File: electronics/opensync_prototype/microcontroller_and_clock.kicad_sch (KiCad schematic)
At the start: 42 parts, among them U2 RP2354_80QFN

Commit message: Backup push
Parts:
- added C? (x2): C, symbol Device:C
- added R?: 1k, symbol Device:R
- added Y?: ABM8-272-T3, ABM8-272-T3:XTAL_ABM8-272-T3, symbol ABM8-272-T3:ABM8-272-T3
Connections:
- net GND: now also Y?.2 (GND), Y?.4 (GND)
- net XIN: now also C?.2, Y?.1
- net XOUT: now also R?.2
- new net: C?.1, C?.1
- new net: C?.2, R?.1, Y?.3
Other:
- note added: "12 MHz Cystal Oscillator"
- note added: "Push Button Boot Select"
- note added: "Push Button Reset"

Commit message: KiCAD backup
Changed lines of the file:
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@@
 	(text "12 MHz Cystal Oscillator"
 		(exclude_from_sim no)
-		(at 41.656 124.968 0)
+		(at 39.624 130.81 0)
 		(effects
 			(font

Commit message: Emergency backup
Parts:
- C10, C11, C12, C13, C14, C15, C16, C17, C2, C3, C6, C7, C8, C9: renamed from C?; footprint (none) -> RP2350_80QFN_minimal:C_0402_1005Metric_small_pads
- C5: renamed from C?; footprint Capacitor_SMD:C_0402_1005Metric -> RP2350_80QFN_minimal:C_0402_1005Metric_small_pads
- L1: renamed from L?; footprint RP2350_80QFN_minimal:L_pol_2016 -> Resistor_SMD:R_0402_1005Metric
- R2: renamed from R?; footprint (none) -> Resistor_SMD:R_0402_1005Metric
- gave numbers to parts that had none: 28

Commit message: Backup copy
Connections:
- net CLOCK_1: now also U2.1 (GPIO4); no longer U2.77 (GPIO0)
- net CLOCK_2: now also U2.2 (GPIO5); no longer U2.78 (GPIO1)
- net CLOCK_3: now also U2.3 (GPIO6); no longer U2.79 (GPIO2)
- net OUTPUT_1: now also U2.21 (GPIO21); no longer U2.6 (GPIO8)
- net OUTPUT_10: now also U2.38 (GPIO30); no longer U2.17 (GPIO17)
- net OUTPUT_11: now also U2.39 (GPIO31); no longer U2.18 (GPIO18)
- net OUTPUT_12: now also U2.40 (GPIO32); no longer U2.19 (GPIO19)
- net OUTPUT_2: now also U2.22 (GPIO22); no longer U2.7 (GPIO9)
- net OUTPUT_3: now also U2.23 (GPIO23); no longer U2.8 (GPIO10)
- net OUTPUT_4: now also U2.25 (GPIO24); no longer U2.9 (GPIO11)
- net OUTPUT_5: now also U2.26 (GPIO25); no longer U2.11 (GPIO12)
- net OUTPUT_6: now also U2.27 (GPIO26); no longer U2.12 (GPIO13)
- net OUTPUT_7: now also U2.28 (GPIO27); no longer U2.13 (GPIO14)
- net OUTPUT_8: now also U2.36 (GPIO28); no longer U2.14 (GPIO15)
- net OUTPUT_9: now also U2.37 (GPIO29); no longer U2.16 (GPIO16)
- net TRIGGER_1: now also U2.18 (GPIO18); no longer U2.1 (GPIO4)
- net TRIGGER_2: now also U2.19 (GPIO19); no longer U2.2 (GPIO5)
- net TRIGGER_3: now also U2.20 (GPIO20); no longer U2.3 (GPIO6)
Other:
- moved on the sheet: R10, R5, R6, R7, R8, R9

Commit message: Emergency backup
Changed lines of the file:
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@@
+		)
+	)
+	(label "OUTPUT_7"
+		(at 172.72 118.11 0)
+		(effects
+			(font
+				(size 1.27 1.27)
+			)
+			(justify left bottom)
+		)
+	)
+	(label "OUTPUT_1"
+		(at 172.72 102.87 0)
+		(effects
+			(font
+				(size 1.27 1.27)
+			)
+			(justify left bottom)
 		)
 	)
@@
 		)
 	)
+	(label "OUTPUT_3"
+		(at 172.72 107.95 0)
+		(effects
+			(font
+				(size 1.27 1.27)
+			)
+			(justify left bottom)
+		)
+	)
+	(label "OUTPUT_5"
+		(at 172.72 113.03 0)
+		(effects
+			(font
+				(size 1.27 1.27)
+			)
+			(justify left bottom)
+		)
+	)
 	(label "CLOCK_2"
 		(at 171.45 62.23 0)
@@
 		)
 	)
+	(label "OUTPUT_2"
+		(at 172.72 105.41 0)
+		(effects
+			(font
+				(size 1.27 1.27)
+			)
+			(justify left bottom)
+		)
+	)
 	(label "RUN"
 		(at 93.98 102.87 0)
@@
 		)
 	)
+	(label "OUTPUT_6"
+		(at 172.8998 115.57 0)
+		(effects
+			(font
+				(size 1.27 1.27)
+			)
+			(justify left bottom)
+		)
+	)
 	(label "QSPL_SS"
 		(at 92.71 60.96 0)
@@
 		)
 	)
+	(label "OUTPUT_9"
+		(at 172.72 123.19 0)
+		(effects
+			(font
+				(size 1.27 1.27)
+			)
+			(justify left bottom)
+		)
+	)
+	(label "TRIGGER_1"
+		(at 172.72 95.25 0)
+		(effects
+			(font
+				(size 1.27 1.27)
+			)
+			(justify left bottom)
+		)
+	)
 	(label "XIN"
 		(at 66.04 135.89 0)
@@
 		)
 	)
+	(label "OUTPUT_12"
+		(at 172.72 130.81 0)
+		(effects
+			(font
+				(size 1.27 1.27)
+			)
+			(justify left bottom)
+		)
+	)
+	(label "OUTPUT_4"
+		(at 172.72 110.49 0)
+		(effects
+			(font
+				(size 1.27 1.27)
+			)
+			(justify left bottom)
+		)
+	)
 	(label "CLOCK_3"
 		(at 171.45 64.77 0)
@@
 		(effects
 			(font
+				(size 1.27 1.27)
+			)
+			(justify left bottom)
+		)
+	)
+	(label "TRIGGER_3"
+		(at 172.72 100.33 0)
+		(effects
+			(font
+				(size 1.27 1.27)
+			)
+			(justify left bottom)
+		)
+	)
+	(label "OUTPUT_11"
+		(at 172.72 128.27 0)
+		(effects
+			(font
+				(size 1.27 1.27)
+			)
+			(justify left bottom)
+		)
+	)
+	(label "TRIGGER_2"
+		(at 172.72 97.79 0)
+		(effects
+			(font
+				(size 1.27 1.27)
+			)
+			(justify left bottom)
+		)
+	)
+	(label "OUTPUT_8"
+		(at 172.8453 120.65 0)
+		(effects
+			(font
+				(size 1.27 1.27)
+			)
+			(justify left bottom)
+		)
+	)
+	(label "OUTPUT_10"
+		(at 172.72 125.73 0)
+		(effects
+			(font

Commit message: Updated PCB design
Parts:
- removed R13, R14, R15, R16, R8, R9: 10k, Resistor_SMD:R_0402_1005Metric, symbol Device:R
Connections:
- net OUTPUT_10 is gone; now on net OUTPUT_6: R22.1, U2.38 (GPIO30)
- net OUTPUT_11 is gone; now on net OUTPUT_7: R23.1, U2.39 (GPIO31)
- net OUTPUT_12 is gone; now on net OUTPUT_8: R24.1, U2.40 (GPIO32)
- net OUTPUT_9 is gone; now on net OUTPUT_5: R21.1, U2.37 (GPIO29)
- net CLOCK_1: now also U2.78 (GPIO1); no longer U2.1 (GPIO4)
- net CLOCK_2: now also U2.79 (GPIO2); no longer U2.2 (GPIO5)
- net CLOCK_3: now also U2.80 (GPIO3); no longer U2.3 (GPIO6)
- net OUTPUT_1: now also R17.1, U2.26 (GPIO25); no longer U2.21 (GPIO21)
- net OUTPUT_2: now also R18.1, U2.27 (GPIO26); no longer U2.22 (GPIO22)
- net OUTPUT_3: now also R19.1, U2.28 (GPIO27); no longer U2.23 (GPIO23)
- net OUTPUT_4: now also R20.1, U2.36 (GPIO28); no longer U2.25 (GPIO24)
- net OUTPUT_5: no longer R17.1, U2.26 (GPIO25)
- net OUTPUT_6: no longer R18.1, U2.27 (GPIO26)
- net OUTPUT_7: no longer R19.1, U2.28 (GPIO27)
- net OUTPUT_8: no longer R20.1, U2.36 (GPIO28)
- net TRIGGER_2: no longer names the net of U2.19 (GPIO19)
- net TRIGGER_3: no longer names the net of U2.20 (GPIO20)
- no-connect marks 37 -> 43

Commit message: GFround and power plane rework
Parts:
- L1: footprint Resistor_SMD:R_0402_1005Metric -> RP2350_80QFN_minimal:L_pol_2016
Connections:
- net VREG_LX: now reaches L1.2, U2.63 (VREG_LX)
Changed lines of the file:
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@@
 		)
 	)
+	(label "VREG_LX"
+		(at 93.98 50.8 0)
+		(effects
+			(font
+				(size 1.27 1.27)
+			)
+			(justify left bottom)
+		)
+	)
 	(label "XOUT"
 		(at 93.98 90.17 0)
@@
 			)
 		)
-		(property "Footprint" "Resistor_SMD:R_0402_1005Metric"
+		(property "Footprint" "RP2350_80QFN_minimal:L_pol_2016"
 			(at 43.18 45.72 0)
 			(effects

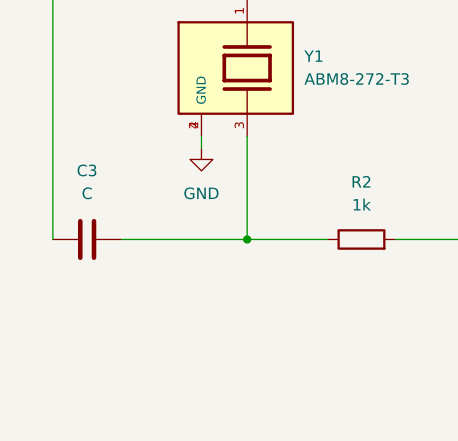
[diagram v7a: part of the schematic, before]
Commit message: Fixed all DRC violations
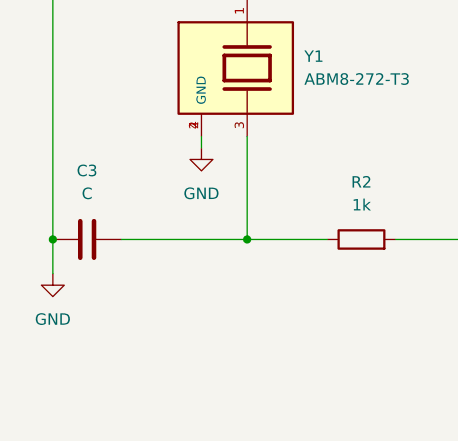
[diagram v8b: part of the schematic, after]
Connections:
- net GND: now also C2.1, C3.1
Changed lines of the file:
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@@
 	)
 	(junction
+		(at 17.78 166.37)
+		(diameter 0)
+		(color 0 0 0 0)
+	)
+	(junction
 		(at 247.65 137.16)
 		(diameter 0)
@@
 	(wire
 		(pts
+			(xy 17.78 166.37) (xy 17.78 170.18)
+		)
+		(stroke
+			(width 0)
+			(type default)
+		)
+	)
+	(wire
+		(pts
 			(xy 218.44 123.19) (xy 218.44 137.16)
 		)
@@
 					(unit 1)
 				)
+			)
+		)
+	)
+	(symbol
+		(lib_id "power:GND")
+		(at 17.78 170.18 0)
+		(unit 1)
+		(exclude_from_sim no)
+		(in_bom yes)
+		(on_board yes)
+		(dnp no)
+		(fields_autoplaced yes)
+		(property "Reference" "#PWR09"
+			(at 17.78 176.53 0)
+			(effects
+				(font
+					(size 1.27 1.27)
+				)
+				(hide yes)
+			)
+		)
+		(property "Value" "GND"
+			(at 17.78 175.26 0)
+			(effects
+				(font
+					(size 1.27 1.27)
+				)
+			)
+		)
+		(property "Footprint" ""
+			(at 17.78 170.18 0)
+			(effects
+				(font
+					(size 1.27 1.27)
+				)
+				(hide yes)
+			)
+		)
+		(property "Datasheet" ""
+			(at 17.78 170.18 0)
+			(effects
+				(font
+					(size 1.27 1.27)
+				)
+				(hide yes)
+			)
+		)
+		(property "Description" "Power symbol creates a global label with name \"GND\" , ground"
+			(at 17.78 170.18 0)
+			(effects
+				(font
+					(size 1.27 1.27)
+				)
+				(hide yes)
+			)
+		)
+		(pin "1"
+		)
+		(instances
+			(project ""
+				(path "/97d97b34-a2f9-4e5e-9870-299ade25a4f4/1cb4b724-597c-4248-8518-89ecf4cdd3ac"
+					(reference "#PWR09")
+					(unit 1)
+				)
